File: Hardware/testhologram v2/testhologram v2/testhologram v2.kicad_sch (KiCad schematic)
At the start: 646 parts, among them J1 USB_C_Receptacle_USB2.0_16P, J2 Conn_01x06_Socket, SW1 SW_Reset, SW2 SW_Boot, U1 SM16106SC, U10 SM16106SC, U11 SM16106SC, U12 SM16106SC, U13 SM16106SC, U14 SM16106SC, U15 SM16106SC, U16 SM16106SC, U17 SM16106SC, U18 SM16106SC, U19 SM16106SC, U2 SM16106SC, U20 SM16106SC, U21 SM16106SC, U22 SM16106SC, U23 SM16106SC, U24 SM16106SC, U25 SM16106SC, U26 SM16106SC, U27 SM16106SC, U28 SM16106SC, U29 SM16106SC, U3 SM16106SC, U30 SM16106SC, U31 SM16106SC, U32 SM16106SC, U33 ESP32-S3-WROOM-1(N16R8), U34 SY8286ARAC, U4 SM16106SC, U5 SM16106SC, U6 SM16106SC, U7 SM16106SC, U8 SM16106SC, U9 SM16106SC

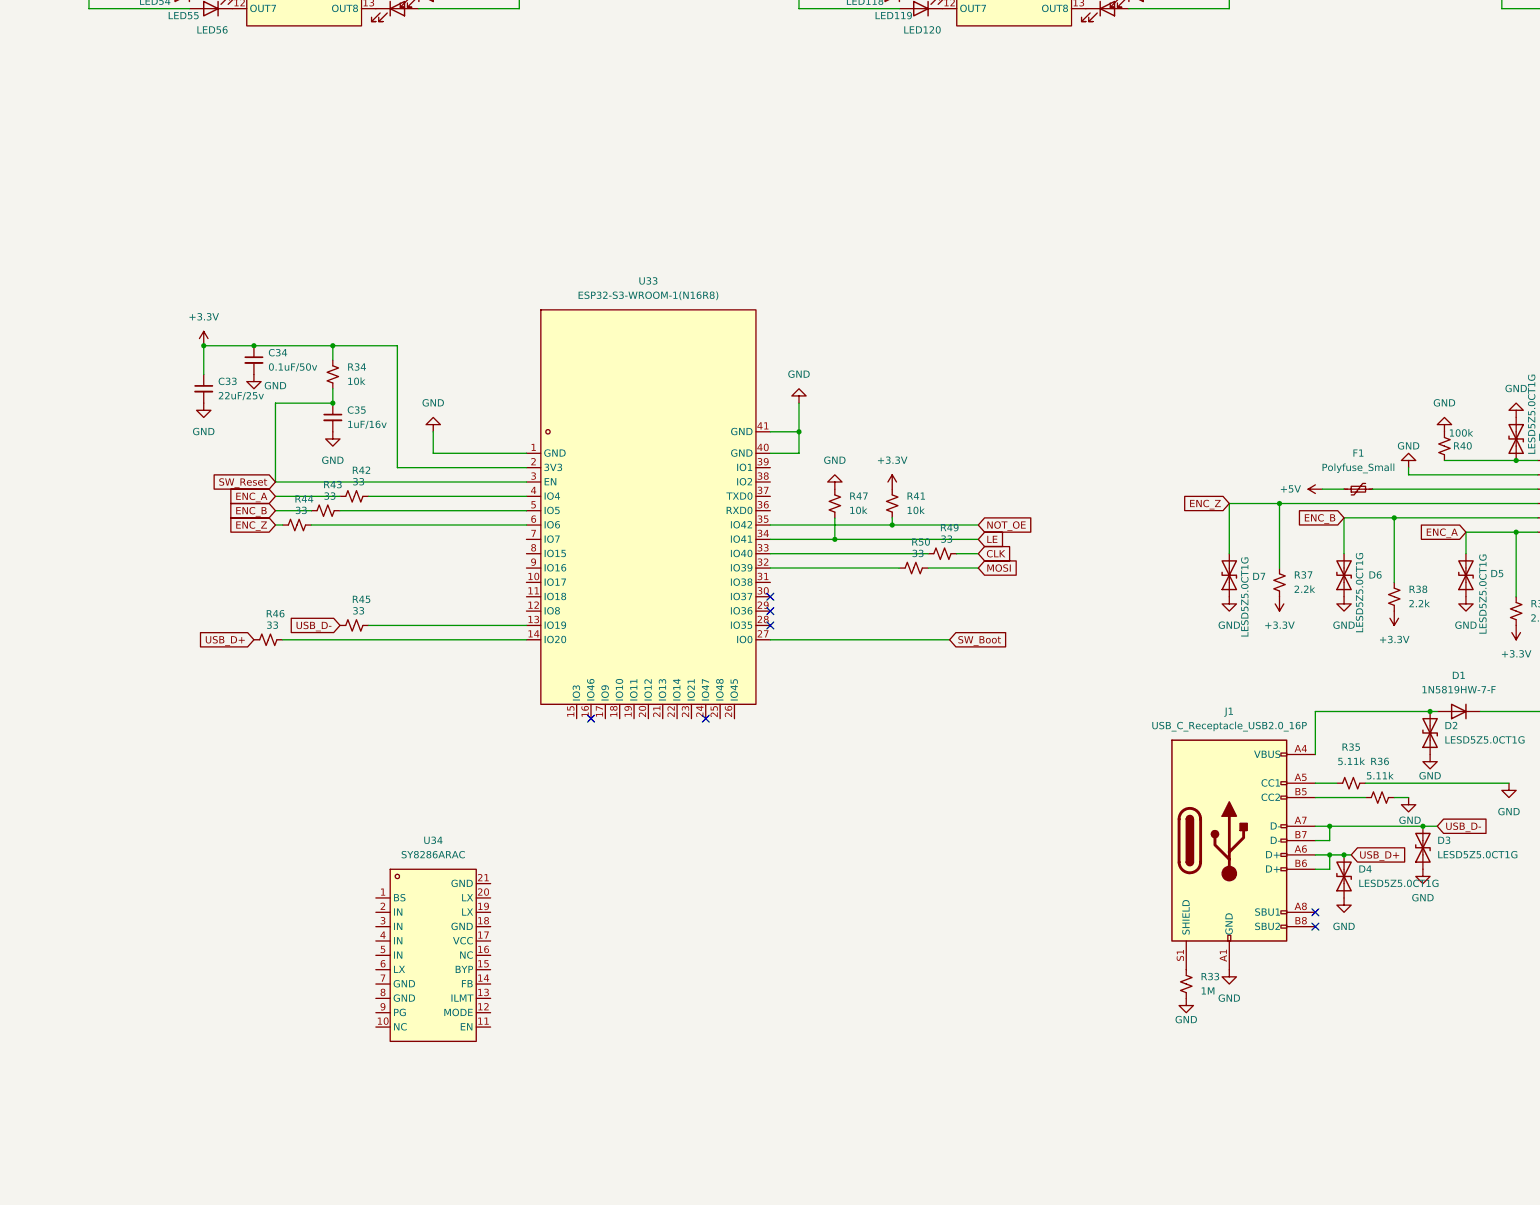
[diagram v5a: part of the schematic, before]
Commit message: added buck converters for 12v->4v and 12v->3.3v. added footprints
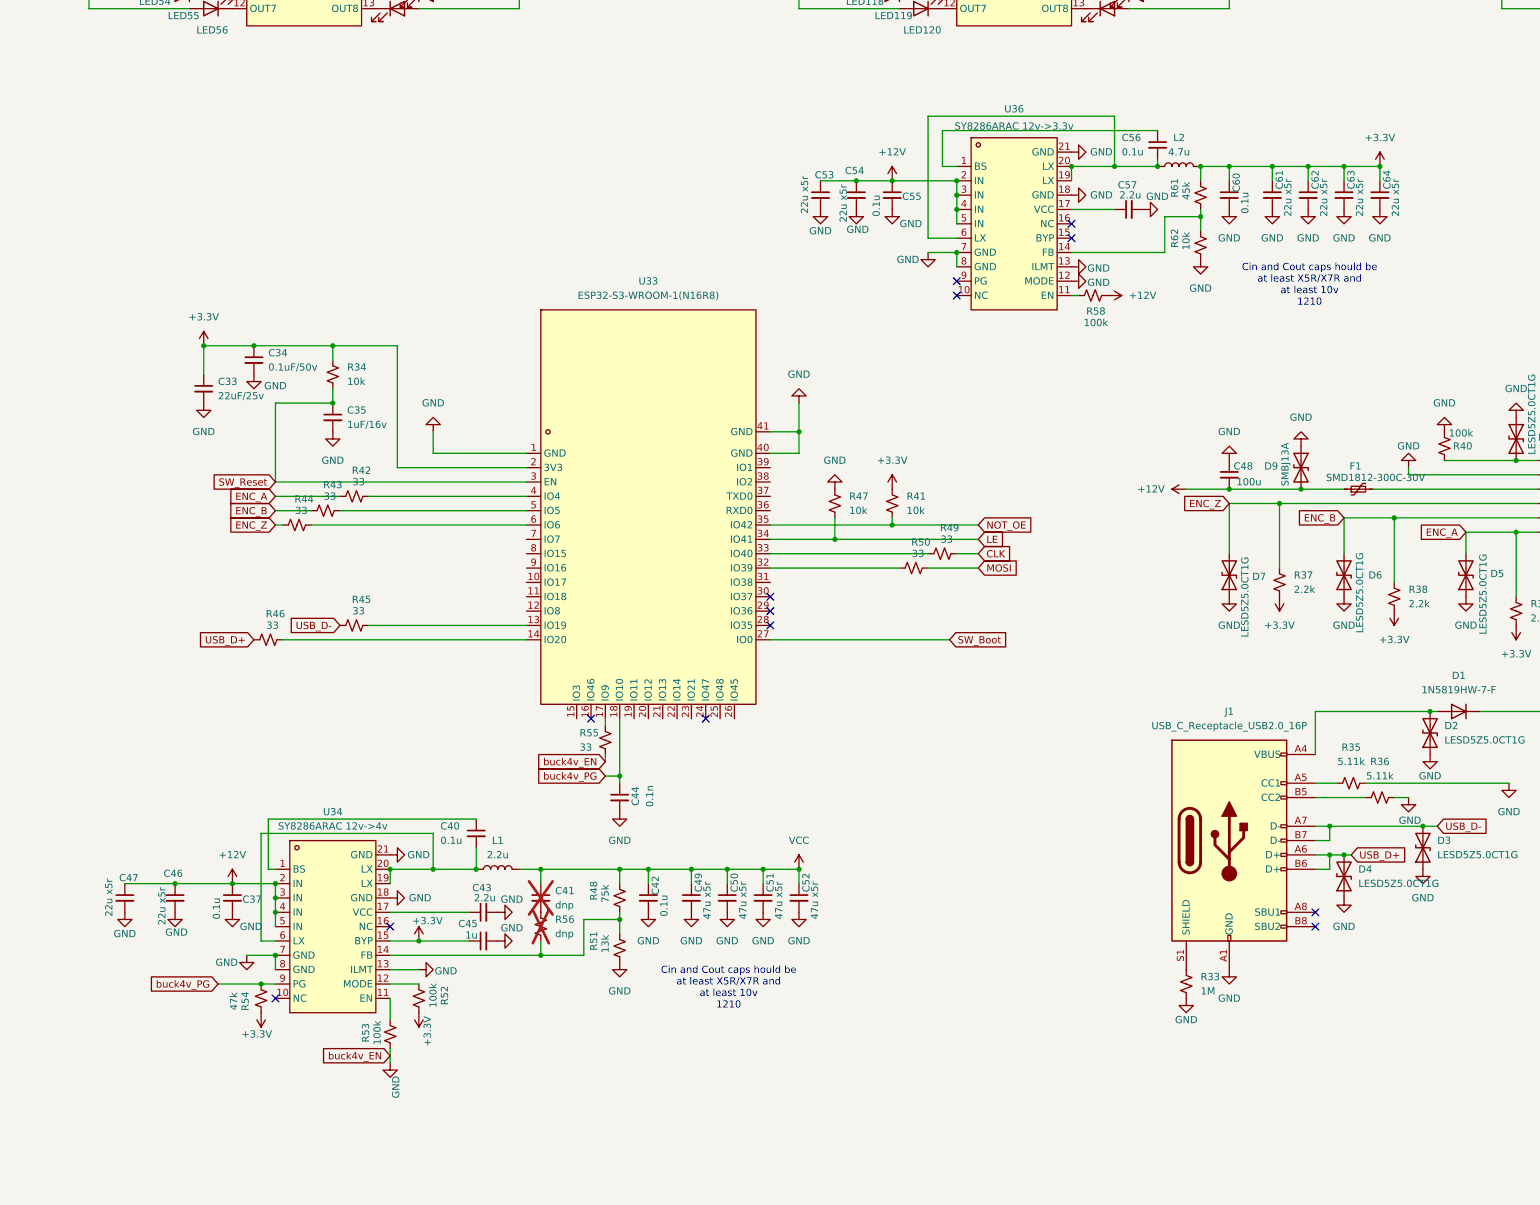
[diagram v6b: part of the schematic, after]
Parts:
- added C37, C40, C42, C55, C56, C60: 0.1u, symbol Device:C_Small
- added C41: dnp, symbol Device:C_Small
- added C43, C57: 2.2u, symbol Device:C_Small
- added C44: 0.1n, symbol Device:C_Small
- added C45: 1u, symbol Device:C_Small
- added C46, C47, C53, C54, C61, C62, C63, C64: 22u x5r, Capacitor_SMD:C_1210_3225Metric, symbol Device:C_Small
- added C48: 100u, easyeda:CAP-SMD_BD6.3-L6.6-W6.6-LS7.3-FD, symbol Device:C_Small
- added C49: 47u x5r, Capacitor_SMD:C_1808_4520Metric, symbol Device:C_Small
- added C50, C51, C52: 47u x5r, Capacitor_SMD:C_1210_3225Metric, symbol Device:C_Small
- added D9: SMBJ13A, symbol Device:D_TVS
- added L1: 2.2u, easyeda:IND-SMD_L10.8-W10.0, symbol Device:L
- added L2: 4.7u, easyeda:IND-SMD_L10.8-W10.0, symbol Device:L
- added R48: 75k, symbol Device:R_Small_US
- added R51: 13k, symbol Device:R_Small_US
- added R52, R53, R58: 100k, symbol Device:R_Small_US
- added R54: 47k, symbol Device:R_Small_US
- added R55: 33, symbol Device:R_Small_US
- added R56: dnp, symbol Device:R_Small_US
- added R61: 45k, symbol Device:R_Small_US
- added R62: 10k, symbol Device:R_Small_US
- added U36: SY8286ARAC 12v->3.3v, easyeda:QFN-20_L3.0-W3.0-P0.45-BL-EP1.0, symbol easyeda:SY8286ARAC
- F1: value Polyfuse_Small -> SMD1812-300C-30V; footprint (none) -> Fuse:Fuse_1812_4532Metric
- U34: value SY8286ARAC -> SY8286ARAC 12v->4v
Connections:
- net +3.3V: now also U34.15 (BYP), C45.1, C60.1, C61.1, C62.1, C63.1, C64.1, L2.2, R52.1, R54.1, R61.1
- net +5V: no longer F1.1
- net GND: now also U34.13 (ILMT), U34.18 (GND), U34.21 (GND), U34.7 (GND), U34.8 (GND), C37.2, C42.2, C43.2, C44.2, C45.2, C46.2, C47.2, C48.1, C49.2, C50.2, C51.2, C52.2, C53.2, C54.2, C55.2, C57.2, C60.2, C61.2, C62.2, C63.2, C64.2, D9.1 (A1), R51.2, R53.2, R55.2, R62.2, U36.12 (MODE), U36.13 (ILMT), U36.18 (GND), U36.21 (GND), U36.7 (GND), U36.8 (GND)
- net VCC: now also C41.1, C42.1, C49.1, C50.1, C51.1, C52.1, L1.2, R48.1
- net at U33.17 (IO9): now also R55.1
- net buck4v_PG: now reaches U33.18 (IO10)
- net buck4v_PG: now also U34.9 (PG), C44.1, R54.2
- net at U34.1 (BS): now also C40.1
- net at U34.11 (EN): now also R53.1
- net at U34.12 (MODE): now also R52.2
- net at U34.14 (FB): now also R48.2, R51.1, R56.2
- net at U34.17 (VCC): now also C43.1
- net at U34.19 (LX): now also U34.20 (LX), U34.6 (LX), C40.2, L1.1
- net +12V: now reaches U34.2 (IN)
- net +12V: now also F1.1, U34.3 (IN), U34.4 (IN), U34.5 (IN), C37.1, C46.1, C47.1, C48.2, C53.1, C54.1, C55.1, D9.2 (A2), R58.1, U36.2 (IN), U36.3 (IN), U36.4 (IN), U36.5 (IN)
- new net: C56.1, U36.1 (BS)
- new net: C56.2, L2.1, U36.19 (LX), U36.20 (LX), U36.6 (LX)
- new net: R58.2, U36.11 (EN)
- new net: C41.2, R56.1
- new net: R61.2, R62.1, U36.14 (FB)
- new net: C57.1, U36.17 (VCC)
- no-connect marks 8 -> 14
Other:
- note added: "Cin and Cout caps hould be at least X5R/X7R and at least 10v 1210"
- moved on the sheet: U34

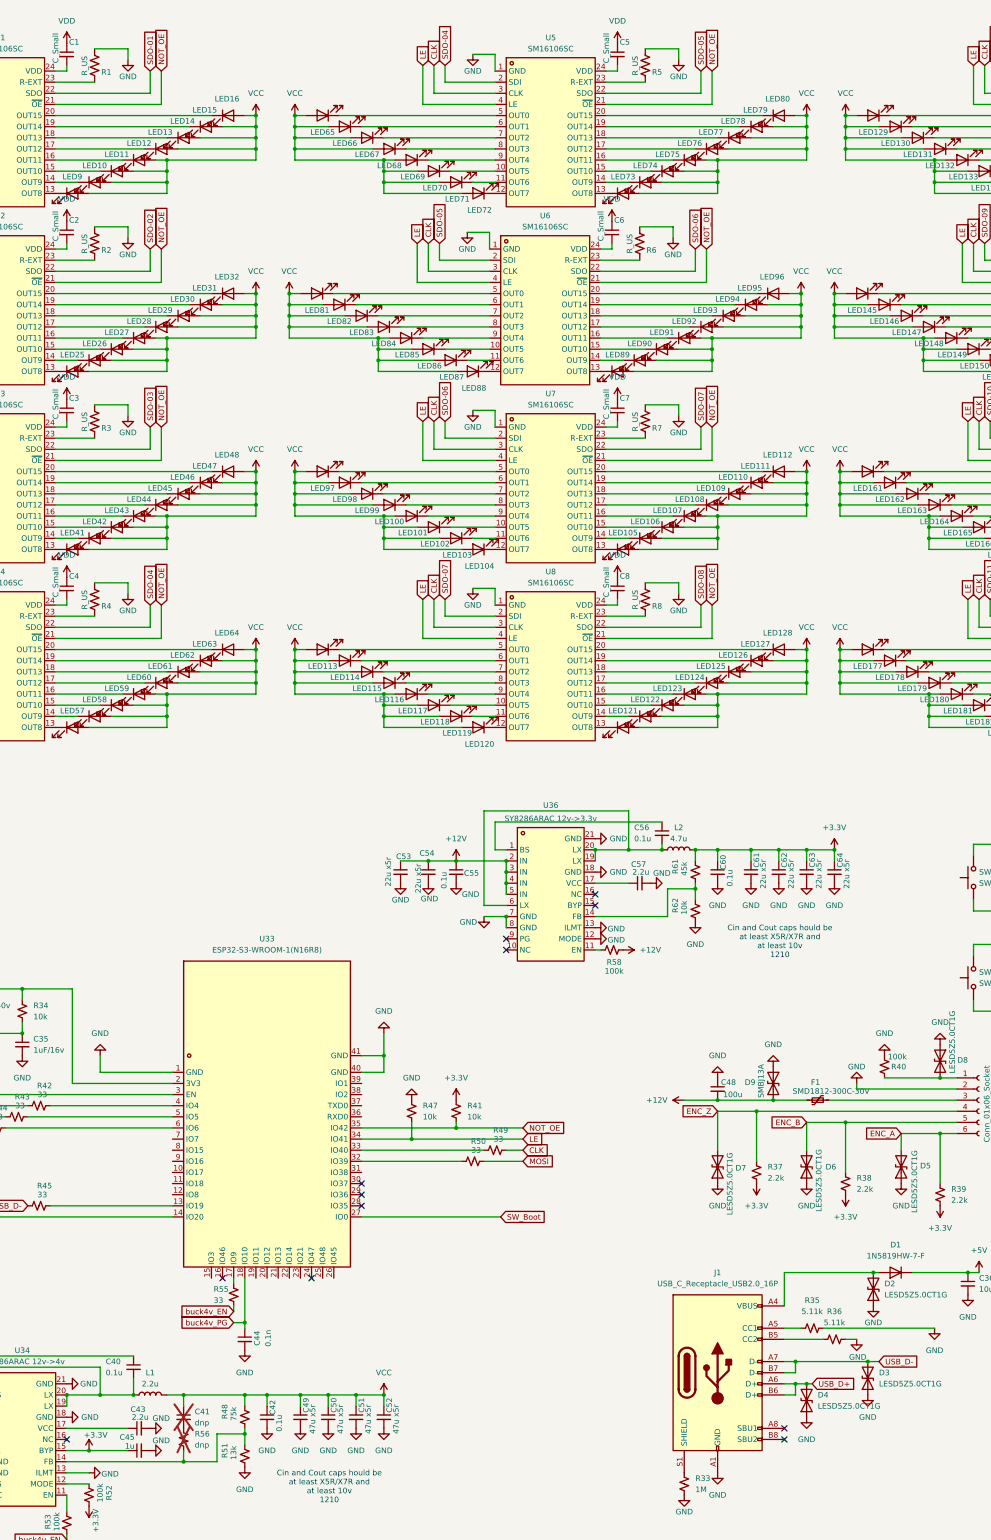
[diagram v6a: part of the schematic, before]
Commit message: added debug leds and debug buttons
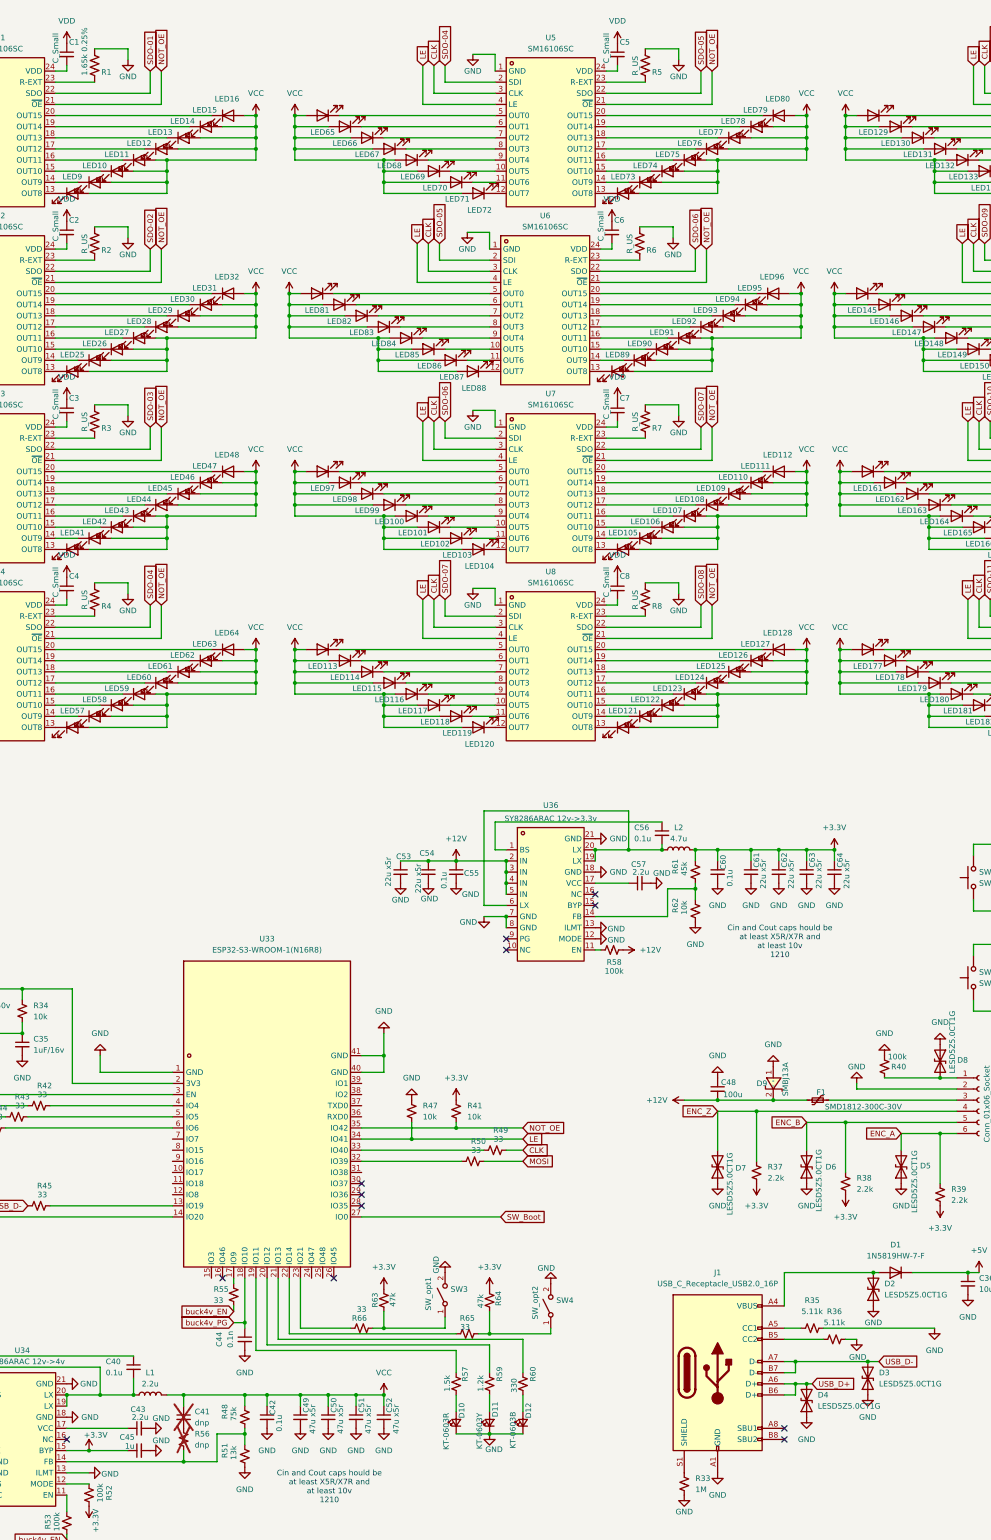
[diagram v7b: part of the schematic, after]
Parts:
- added D10: KT-0603R, symbol Device:LED_Small
- added D11: KT-0603Y, symbol Device:LED_Small
- added D12: KT-0603B, symbol Device:LED_Small
- added R57: 1.5k, symbol Device:R_Small_US
- added R59: 1.2k, symbol Device:R_Small_US
- added R60: 330, symbol Device:R_Small_US
- added R63, R64: 47k, symbol Device:R_Small_US
- added R65, R66: 33, symbol Device:R_Small_US
- added SW3: SW_opt1, easyeda:KEY-SMD_L4.0-W3.0-LS4.9-1, symbol Switch:SW_SPST
- added SW4: SW_opt2, easyeda:KEY-SMD_L4.0-W3.0-LS4.9-1, symbol Switch:SW_SPST
- D7: footprint (none) -> easyeda:SOD-523_L1.2-W0.8-LS1.6-BI
- D9: footprint (none) -> easyeda:SMB_L4.6-W3.6-LS5.3-RD; symbol Device:D_TVS -> easyeda:SMBJ13A; LCSC Part (none) -> C10209
- R1: value R_US -> 1.65k 0.25%
- U1, U10, U11, U12, U13, U14, U15, U16, U17, U18, U19, U2, U20, U21, U22, U23, U24, U25, U26, U27, U28, U29, U3, U30, U31, U32, U4, U5, U6, U7, U8, U9: footprint sm16206s:QSOP-24_L8.7-W4.0-P0.64-LS6.0-BL -> easyeda2kicad:QSOP-24_L8.7-W4.0-P0.65-LS6.0-BL
- U33: footprint esp32-s3-wroom-1:WIRELM-SMD_ESP32-S3-WROOM-1 -> easyeda2kicad:WIRELM-SMD_ESP32-S3-WROOM-1
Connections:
- net +3.3V: now also R63.2, R64.1
- net GND: now also D10.1 (K), D11.1 (K), D12.1 (K), SW3.2 (B), SW4.2 (B)
- net at U33.19 (IO11): now also R57.1
- net at U33.20 (IO12): now also R59.1
- net at U33.21 (IO13): now also R60.1
- net at U33.22 (IO14): now also R65.2
- net at U33.23 (IO21): now also R66.1
- new net: D12.2 (A), R60.2
- new net: D11.2 (A), R59.2
- new net: R64.2, R65.1, SW4.1 (A)
- new net: R63.1, R66.2, SW3.1 (A)
- new net: D10.2 (A), R57.2

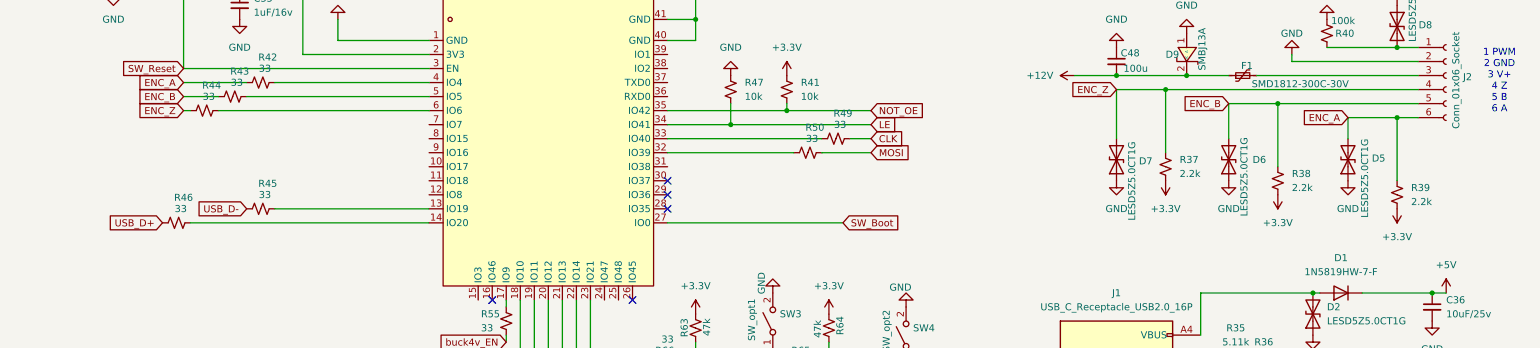
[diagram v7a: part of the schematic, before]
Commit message: adding footprints
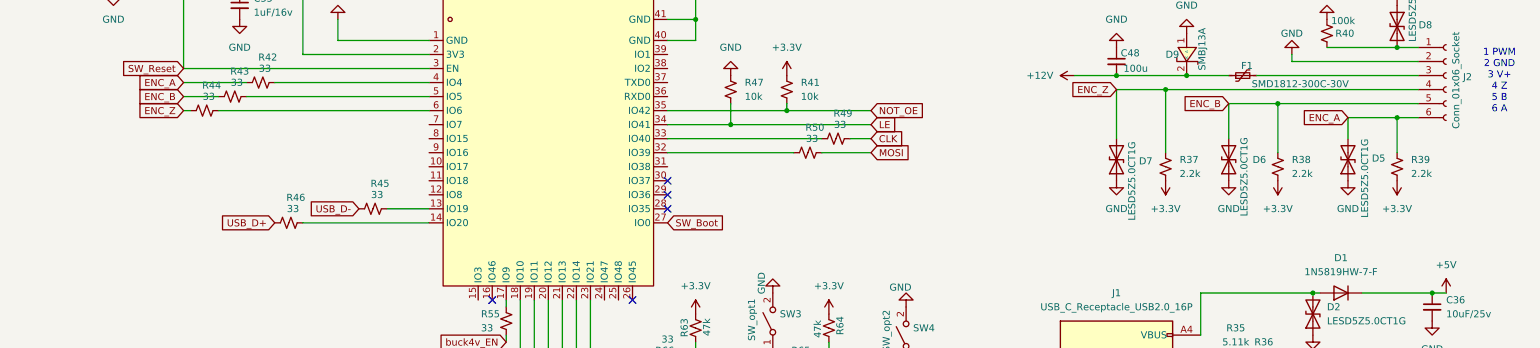
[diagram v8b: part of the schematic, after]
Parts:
- C33, C36: footprint (none) -> Capacitor_SMD:C_0805_2012Metric
- C34, C37, C38, C39, C40, C42, C44, C55, C56, C60: footprint (none) -> Capacitor_SMD:C_0402_1005Metric
- C35, C41, C43, C45, C57: footprint (none) -> Capacitor_SMD:C_0603_1608Metric
- C49: footprint Capacitor_SMD:C_1808_4520Metric -> Capacitor_SMD:C_1210_3225Metric
- D1: footprint (none) -> easyeda:SOD-123_L2.7-W1.6-LS3.7-RD
- D10, D11, D12: footprint (none) -> LED_SMD:LED_0603_1608Metric
- D2, D3, D4, D5, D6, D8: footprint (none) -> easyeda:SOD-523_L1.2-W0.8-LS1.6-BI
- J1: footprint (none) -> easyeda:USB-C-SMD_TYPE-C-6PIN-2MD-073
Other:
- moved on the sheet: R38, R39, R45, R46
